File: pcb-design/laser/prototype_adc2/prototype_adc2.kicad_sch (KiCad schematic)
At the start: 55 parts, among them J1 Conn_01x01_Socket, J2 Conn_01x01_Socket, J3 Conn_01x01_Socket, J4 Conn_01x01_Socket, J5 Conn_01x01_Socket, J6 Conn_01x01_Socket, J7 Conn_01x01_Socket, J8 Conn_01x01_Socket, J9 Conn_01x01_Socket, U2 MCP1541T-I_TT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

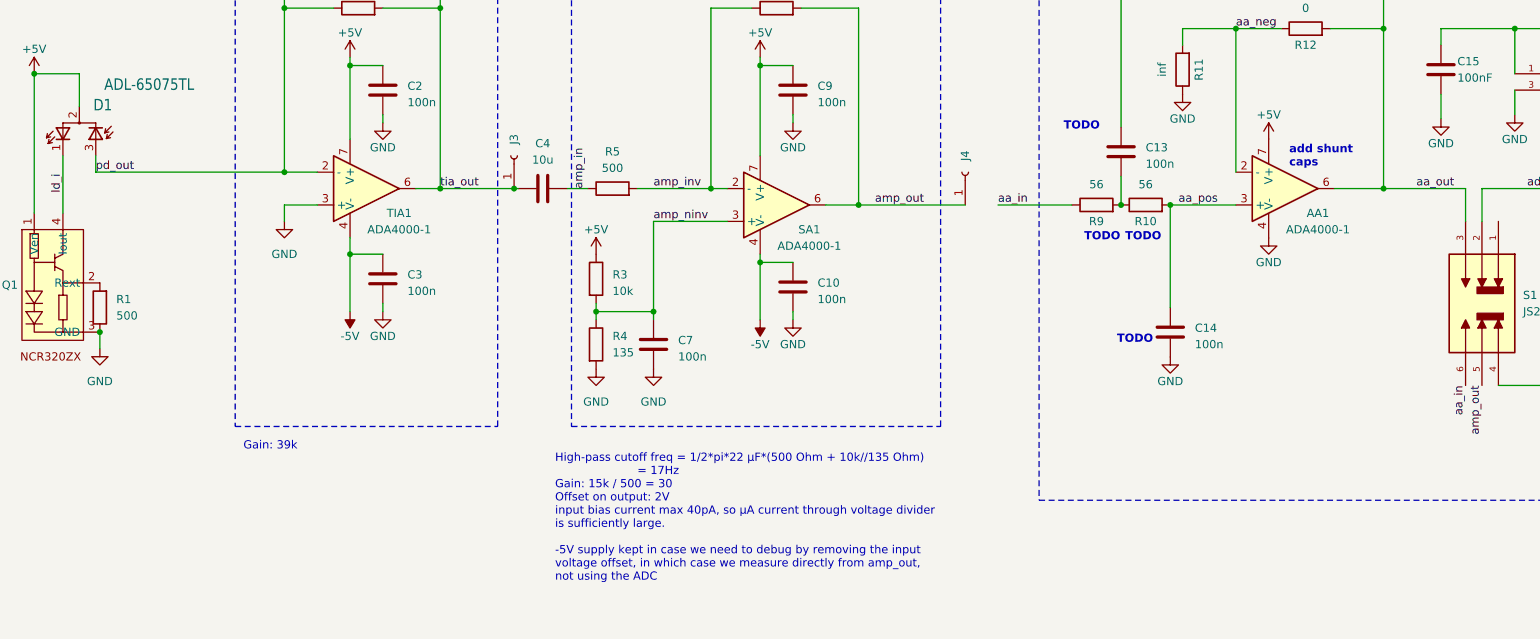
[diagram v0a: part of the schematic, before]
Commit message: laser schematic AA cutoff fix
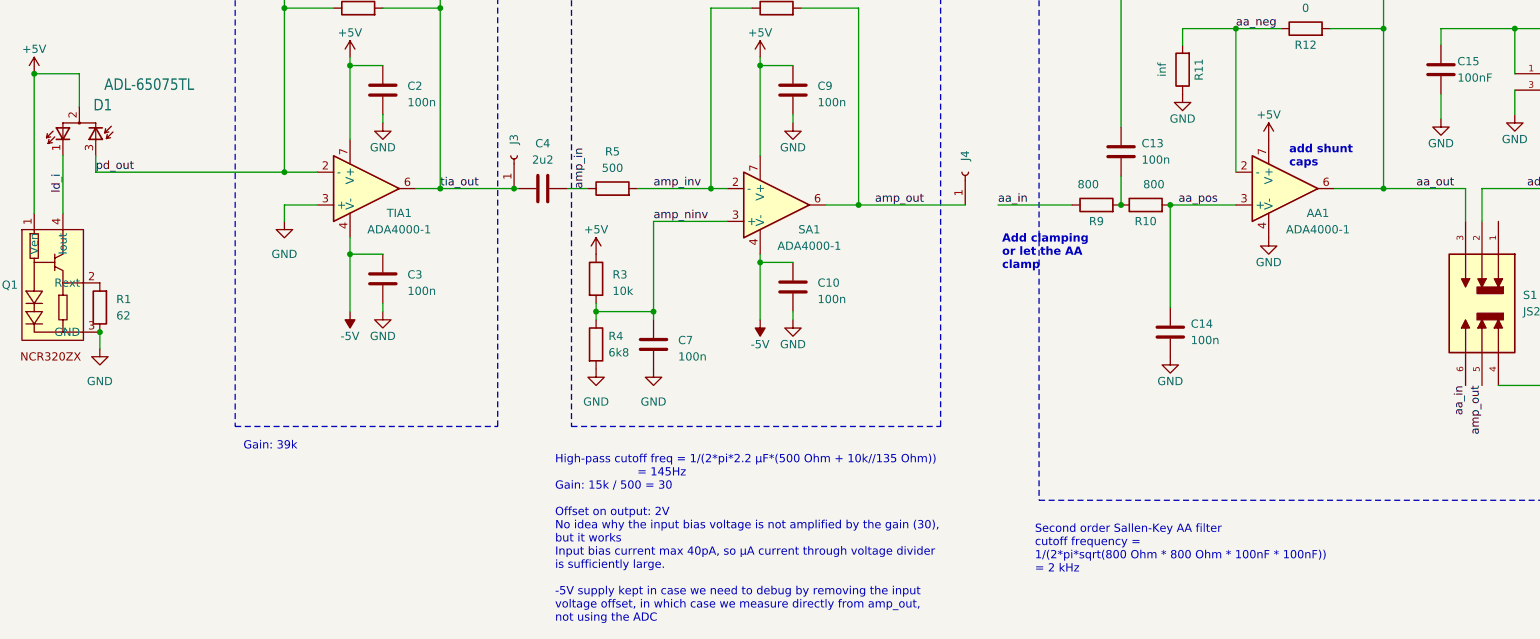
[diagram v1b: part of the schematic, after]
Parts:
- C4: value 10u -> 2u2
- R1: value 500 -> 62
- R10, R9: value 56 -> 800
- R4: value 135 -> 6k8
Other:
- note added: "Add clamping or let the AA clamp"
- note added: "High-pass cutoff freq = 1/(2*pi*2.2 µF*(500 Ohm + 10k//135 Ohm)) = 145Hz Gain: 15k / 500 = 30 Offset on output: 2V No idea why the input bias voltage is not amplified by the gain (30), but it works Input bias current max 40pA, so µA current through voltage divider is sufficiently large. -5V supply kept in case we need to debug by removing the input voltage offset, in which case we measure directl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"
- note added: "Second order Sallen-Key AA filter cutoff frequency = 1/(2*pi*sqrt(800 Ohm * 800 Ohm * 100nF * 100nF)) = 2 kHz"
- note removed: "High-pass cutoff freq = 1/2*pi*22 µF*(500 Ohm + 10k//135 Ohm) = 17Hz Gain: 15k / 500 = 30 Offset on output: 2V input bias current max 40pA, so µA current through voltage divider is sufficiently large. -5V supply kept in case we need to debug by removing the input voltage offset, in which case we measure directly from amp_out, not using the ADC"
- note removed: "TODO"
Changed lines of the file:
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@@
     (effects (font (size 1.27 1.27) (thickness 0.254) bold) (justify left bottom))
   )
-  (text "TODO" (at 205.105 145.415 0)
-    (effects (font (size 1.27 1.27) (thickness 0.254) bold (color 255 0 13 1)) (justify left bottom))
-  )
-  (text "TODO" (at 214.63 162.56 0)
-    (effects (font (size 1.27 1.27) (thickness 0.254) bold (color 255 0 13 1)) (justify left bottom))
+  (text "Add clamping\nor let the AA\nclamp" (at 195.58 167.005 0)
+    (effects (font (size 1.27 1.27) (thickness 0.254) bold (color 255 3 20 1)) (justify left bottom))
+  )
+  (text "Second order Sallen-Key AA filter\ncutoff frequency = \n1/(2*pi*sqrt(800 Ohm * 800 Ohm * 100nF * 100nF))\n= 2 kHz"
+    (at 200.66 213.995 0)
+    (effects (font (size 1.27 1.27)) (justify left bottom))
   )
   (text "2nd order Sallen-Key\nanti-aliasing filter" (at 210.185 119.38 0)
     (effects (font (size 1.27 1.27) (thickness 0.254) bold) (justify left bottom))
   )
-  (text "High-pass cutoff freq = 1/2*pi*22 µF*(500 Ohm + 10k//135 Ohm) \n                       = 17Hz\nGain: 15k / 500 = 30\nOffset on output: 2V\ninput bias current max 40pA, so µA current through voltage divider \nis sufficiently large.\n\n-5V supply kept in case we need to debug by removing the input \nvoltage offset, in which case we measure directly from amp_out,\nnot using the ADC"
-    (at 126.365 215.265 0)
+  (text "High-pass cutoff freq = 1/(2*pi*2.2 µF*(500 Ohm + 10k//135 Ohm)) \n                       = 145Hz\nGain: 15k / 500 = 30\n\nOffset on output: 2V\nNo idea why the input bias voltage is not amplified by the gain (30),\nbut it works\nInput bias current max 40pA, so µA current through voltage divider \nis sufficiently large.\n\n-5V supply kept in case we need to debug by removing the input \nvoltage offset, in which case we measure directly from amp_out,\nnot using the ADC"
+    (at 126.365 221.615 0)
     (effects (font (size 1.27 1.27)) (justify left bottom))
   )
@@
   (text "24 V to +5 V and -5 V (max. 100 mA per rail)" (at 76.962 98.806 0)
     (effects (font (size 1.27 1.27)) (justify left bottom))
-  )
-  (text "TODO" (at 213.36 178.435 0)
-    (effects (font (size 1.27 1.27) (thickness 0.254) bold (color 255 0 13 1)) (justify left bottom))
   )
   (text "Stabilizing cap." (at 78.232 112.649 0)
@@
     (effects (font (size 1.27 1.27) (thickness 0.254) bold) (justify left bottom))
   )
-  (text "TODO" (at 208.28 162.56 0)
-    (effects (font (size 1.27 1.27) (thickness 0.254) bold (color 255 0 13 1)) (justify left bottom))
-  )
   (text "Power supply" (at 76.835 59.69 0)
     (effects (font (size 1.27 1.27) (thickness 0.254) bold) (justify left bottom))
@@
       (effects (font (size 1.27 1.27)))
     )
-    (property "Value" "56" (at 217.805 153.67 90)
+    (property "Value" "800" (at 219.075 153.67 90)
       (effects (font (size 1.27 1.27)))
     )
@@
   (symbol (lib_id "Device:R") (at 132.715 178.435 0) (unit 1)
     (in_bom yes) (on_board yes) (dnp no) (fields_autoplaced)
-    (property "Reference" "R4" (at 135.255 177.165 0)
-      (effects (font (size 1.27 1.27)) (justify left))
-    )
-    (property "Value" "135" (at 135.255 179.705 0)
+    (property "Reference" "R4" (at 134.62 177.165 0)
+      (effects (font (size 1.27 1.27)) (justify left))
+    )
+    (property "Value" "6k8" (at 134.62 179.705 0)
       (effects (font (size 1.27 1.27)) (justify left))
     )
@@
       (effects (font (size 1.27 1.27)))
     )
-    (property "Value" "10u" (at 124.46 149.86 90)
+    (property "Value" "2u2" (at 124.46 149.86 90)
       (effects (font (size 1.27 1.27)))
     )
@@
       (effects (font (size 1.27 1.27)))
     )
-    (property "Value" "56" (at 210.185 153.67 90)
+    (property "Value" "800" (at 208.915 153.67 90)
       (effects (font (size 1.27 1.27)))
     )
@@
   (symbol (lib_id "Device:C") (at 221.615 176.53 0) (unit 1)
     (in_bom yes) (on_board yes) (dnp no) (fields_autoplaced)
-    (property "Reference" "C14" (at 225.425 175.895 0)
-      (effects (font (size 1.27 1.27)) (justify left))
-    )
-    (property "Value" "100n" (at 225.425 178.435 0)
+    (property "Reference" "C14" (at 224.79 175.26 0)
+      (effects (font (size 1.27 1.27)) (justify left))
+    )
+    (property "Value" "100n" (at 224.79 177.8 0)
       (effects (font (size 1.27 1.27)) (justify left))
     )
@@
   (symbol (lib_id "Device:C") (at 213.995 148.59 0) (unit 1)
     (in_bom yes) (on_board yes) (dnp no) (fields_autoplaced)
-    (property "Reference" "C13" (at 217.805 147.955 0)
-      (effects (font (size 1.27 1.27)) (justify left))
-    )
-    (property "Value" "100n" (at 217.805 150.495 0)
+    (property "Reference" "C13" (at 217.17 147.32 0)
+      (effects (font (size 1.27 1.27)) (justify left))
+    )
+    (property "Value" "100n" (at 217.17 149.86 0)
       (effects (font (size 1.27 1.27)) (justify left))
     )
@@
       (effects (font (size 1.27 1.27)) (justify right))
     )
-    (property "Value" "500" (at 58.42 173.99 0)
+    (property "Value" "62" (at 58.42 173.99 0)
       (effects (font (size 1.27 1.27)) (justify right))
     )
